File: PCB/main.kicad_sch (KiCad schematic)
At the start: 11 parts, among them Q3 BC337, SW1 config, U1 ESP32-S2-DevKitM

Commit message: First uncompleted release
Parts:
- U1: footprint PCM_Espressif:ESP32-S2-DevKitM -> esp32_dk:ESP32-S2-DevKitM
- renumbered Q3 to Q1, R2 to R1, R7 to R2, R6 to R5
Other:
- added sheet Front outputs (mbes_front_outputs.kicad_sch)
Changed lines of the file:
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@@
 		(on_board yes)
 		(dnp no)
-		(property "Reference" "#PWR01"
+		(property "Reference" "#PWR02"
 			(at 173.99 42.926 0)
 			(effects
@@
 			(project "pcb-a"
 				(path "/709d0967-afe5-49d3-92a5-d2bb94550bdb"
-					(reference "#PWR01")
+					(reference "#PWR02")
 					(unit 1)
 				)
@@
 		(on_board yes)
 		(dnp no)
-		(property "Reference" "R7"
+		(property "Reference" "R2"
 			(at 180.594 50.0888 90)
 			(effects
@@
 			(project "pcb-a"
 				(path "/709d0967-afe5-49d3-92a5-d2bb94550bdb"
-					(reference "R7")
+					(reference "R2")
 					(unit 1)
 				)
@@
 			)
 		)
-		(property "Footprint" "PCM_Espressif:ESP32-S2-DevKitM"
+		(property "Footprint" "esp32_dk:ESP32-S2-DevKitM"
 			(at 135.128 147.32 0)
 			(effects
@@
 		(on_board yes)
 		(dnp no)
-		(property "Reference" "#PWR0104"
+		(property "Reference" "#PWR04"
 			(at 233.172 109.22 0)
 			(effects
@@
 			(project "pcb-a"
 				(path "/709d0967-afe5-49d3-92a5-d2bb94550bdb"
-					(reference "#PWR0104")
+					(reference "#PWR04")
 					(unit 1)
 				)
@@
 		(on_board yes)
 		(dnp no)
-		(property "Reference" "R2"
+		(property "Reference" "R1"
 			(at 117.602 45.1612 90)
 			(effects
@@
 			(project "pcb-a"
 				(path "/709d0967-afe5-49d3-92a5-d2bb94550bdb"
-					(reference "R2")
+					(reference "R1")
 					(unit 1)
 				)
@@
 		(on_board yes)
 		(dnp no)
-		(property "Reference" "R6"
+		(property "Reference" "R5"
 			(at 209.296 27.6352 90)
 			(effects
@@
 			(project "pcb-a"
 				(path "/709d0967-afe5-49d3-92a5-d2bb94550bdb"
-					(reference "R6")
+					(reference "R5")
 					(unit 1)
 				)
@@
 		(on_board yes)
 		(dnp no)
-		(property "Reference" "#PWR02"
+		(property "Reference" "#PWR03"
 			(at 188.976 62.23 0)
 			(effects
@@
 			(project "pcb-a"
 				(path "/709d0967-afe5-49d3-92a5-d2bb94550bdb"
-					(reference "#PWR02")
+					(reference "#PWR03")
 					(unit 1)
 				)
@@
 		(on_board yes)
 		(dnp no)
-		(property "Reference" "Q3"
+		(property "Reference" "Q1"
 			(at 189.2301 30.8864 0)
 			(effects
@@
 			(project "pcb-a"
 				(path "/709d0967-afe5-49d3-92a5-d2bb94550bdb"
-					(reference "Q3")
+					(reference "Q1")
 					(unit 1)
 				)
@@
 		(on_board yes)
 		(dnp no)
-		(property "Reference" "#PWR0103"
+		(property "Reference" "#PWR01"
 			(at 132.588 150.114 0)
 			(effects
@@
 			(project "pcb-a"
 				(path "/709d0967-afe5-49d3-92a5-d2bb94550bdb"
-					(reference "#PWR0103")
+					(reference "#PWR01")
 					(unit 1)
 				)
@@
 	)
 	(sheet
-		(at 22.098 20.066)
-		(size 33.02 9.144)
+		(at 61.468 20.066)
+		(size 29.21 9.144)
 		(exclude_from_sim no)
 		(in_bom yes)
@@
 			(color 0 0 0 0.0000)
 		)
+		(property "Sheetname" "Front outputs"
+			(at 61.468 19.3544 0)
+			(effects
+				(font
+					(size 1.27 1.27)
+				)
+				(justify left bottom)
+			)
+		)
+		(property "Sheetfile" "mbes_front_outputs.kicad_sch"
+			(at 61.468 29.7946 0)
+			(effects
+				(font
+					(size 1.27 1.27)
+				)
+				(justify left top)
+			)
+		)
+		(instances
+			(project "main"
+				(path "/709d0967-afe5-49d3-92a5-d2bb94550bdb"
+					(page "3")
+				)
+			)
+		)
+	)
+	(sheet
+		(at 22.098 20.066)
+		(size 33.02 9.144)
+		(exclude_from_sim no)
+		(in_bom yes)
+		(on_board yes)
+		(dnp no)
+		(fields_autoplaced yes)
+		(stroke
+			(width 0.1524)
+			(type solid)
+		)
+		(fill
+			(color 0 0 0 0.0000)
+		)
 		(property "Sheetname" "mbes_pcbA_connectors"
 			(at 22.098 19.3544 0)
@@
 		)
 		(instances
-			(project "pcb-a"
+			(project "main"
 				(path "/709d0967-afe5-49d3-92a5-d2bb94550bdb"
 					(page "3")

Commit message: Enhancement: the last BC337 has been replaced by a BC817
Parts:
- removed Q1: BC337, Package_TO_SOT_THT:TO-92_Inline_Wide, symbol Transistor_BJT:BC337
- added Q19: BC817, Package_TO_SOT_SMD:SOT-23, symbol Transistor_BJT:BC817
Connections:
- net GND: now also Q19.2 (E)
- net c_startEngine: now also Q19.3 (C)
- net at R2.1: now also Q19.1 (B)
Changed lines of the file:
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@@
-	)
-	(symbol
-		(lib_id "Transistor_BJT:BC337")
-		(at 187.96 35.814 270)
-		(mirror x)
-		(unit 1)
-		(exclude_from_sim no)
-		(in_bom yes)
-		(on_board yes)
-		(dnp no)
-		(property "Reference" "Q1"
-			(at 189.2301 30.8864 0)
-			(effects
-				(font
-					(size 1.27 1.27)
-				)
-				(justify left)
-				(hide yes)
-			)
-		)
-		(property "Value" "BC337"
-			(at 184.658 30.5308 90)
-			(effects
-				(font
-					(size 1.27 1.27)
-				)
-				(justify left)
-			)
-		)
-		(property "Footprint" "Package_TO_SOT_THT:TO-92_Inline_Wide"
-			(at 186.055 30.734 0)
-			(effects
-				(font
-					(size 1.27 1.27)
-					(italic yes)
-				)
-				(justify left)
-				(hide yes)
-			)
-		)
-		(property "Datasheet" "https://diotec.com/tl_files/diotec/files/pdf/datasheets/bc337.pdf"
-			(at 187.96 35.814 0)
-			(effects
-				(font
-					(size 1.27 1.27)
-				)
-				(justify left)
-				(hide yes)
-			)
-		)
-		(property "Description" ""
-			(at 187.96 35.814 0)
-			(effects
-				(font
-					(size 1.27 1.27)
-				)
-				(hide yes)
-			)
-		)
-		(pin "1"
-		)
-		(pin "2"
-		)
-		(pin "3"
-		)
-		(instances
-			(project "pcb-a"
-				(path "/709d0967-afe5-49d3-92a5-d2bb94550bdb"
-					(reference "Q1")
-					(unit 1)
-				)
-			)
-		)
 	)
 	(symbol
@@
 					(unit 1)
 				)
+			)
+		)
+	)
+	(symbol
+		(lib_id "Transistor_BJT:BC817")
+		(at 187.96 35.814 270)
+		(mirror x)
+		(unit 1)
+		(exclude_from_sim no)
+		(in_bom yes)
+		(on_board yes)
+		(dnp no)
+		(fields_autoplaced yes)
+		(property "Reference" "Q19"
+			(at 187.96 26.416 90)
+			(effects
+				(font
+					(size 1.27 1.27)
+				)
+				(hide yes)
+			)
+		)
+		(property "Value" "BC817"
+			(at 187.96 28.956 90)
+			(effects
+				(font
+					(size 1.27 1.27)
+				)
+			)
+		)
+		(property "Footprint" "Package_TO_SOT_SMD:SOT-23"
+			(at 186.055 30.734 0)
+			(effects
+				(font
+					(size 1.27 1.27)
+					(italic yes)
+				)
+				(justify left)
+				(hide yes)
+			)
+		)
+		(property "Datasheet" "https://www.onsemi.com/pub/Collateral/BC818-D.pdf"
+			(at 187.96 35.814 0)
+			(effects
+				(font
+					(size 1.27 1.27)
+				)
+				(justify left)
+				(hide yes)
+			)
+		)
+		(property "Description" "0.8A Ic, 45V Vce, NPN Transistor, SOT-23"
+			(at 187.96 35.814 0)
+			(effects
+				(font
+					(size 1.27 1.27)
+				)
+				(hide yes)
+			)
+		)
+		(pin "2"
+		)
+		(pin "1"
+		)
+		(pin "3"
+		)
+		(instances
+			(project ""
+				(path "/709d0967-afe5-49d3-92a5-d2bb94550bdb"
+					(reference "Q19")
+					(unit 1)
+				)

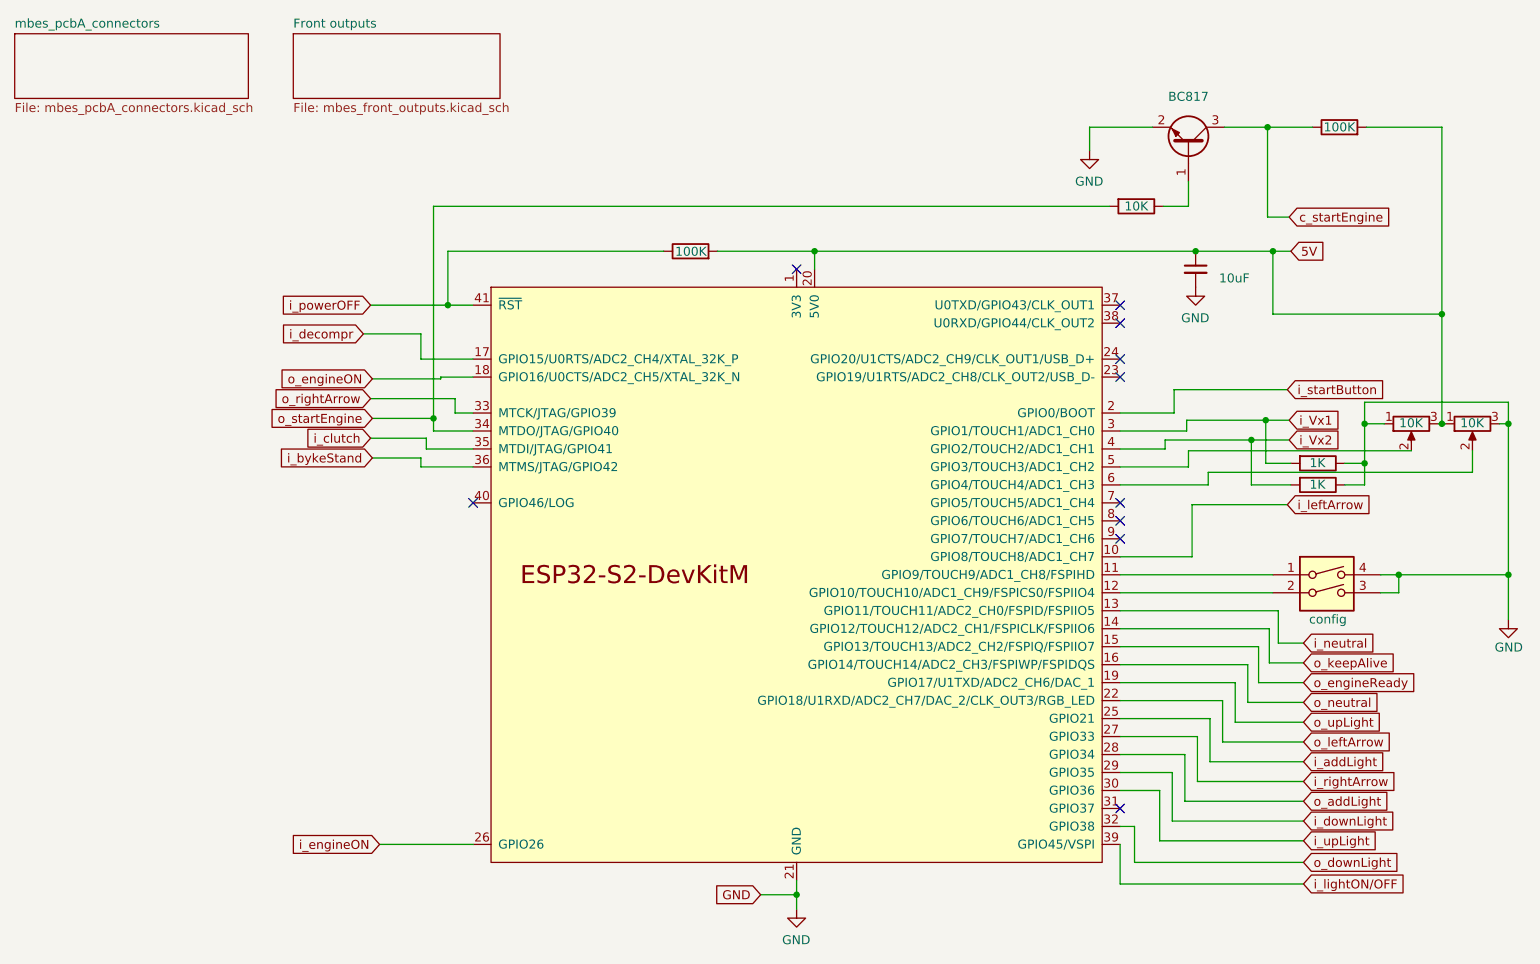
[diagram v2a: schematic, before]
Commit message: Many fixes and changes
- Electric schema and PCB changes:
	- To avoid unwanted service starting (lights, electric start engine....), the signals from the motorbike's front side to
	  the rear one, are no more connedted to the FET's gate directly. There is a second stage realized with PNPs transistors,
	  now. It is a more stable and safe solution.

- In the shcema:
	- All the c_<signal> symbols have been splitted in ci_<signal> and co_<signal>, and the symbols direction (input/output)
	  have been fixed
	- To get a more readable schema, the c*_<signal> symbols have a different color
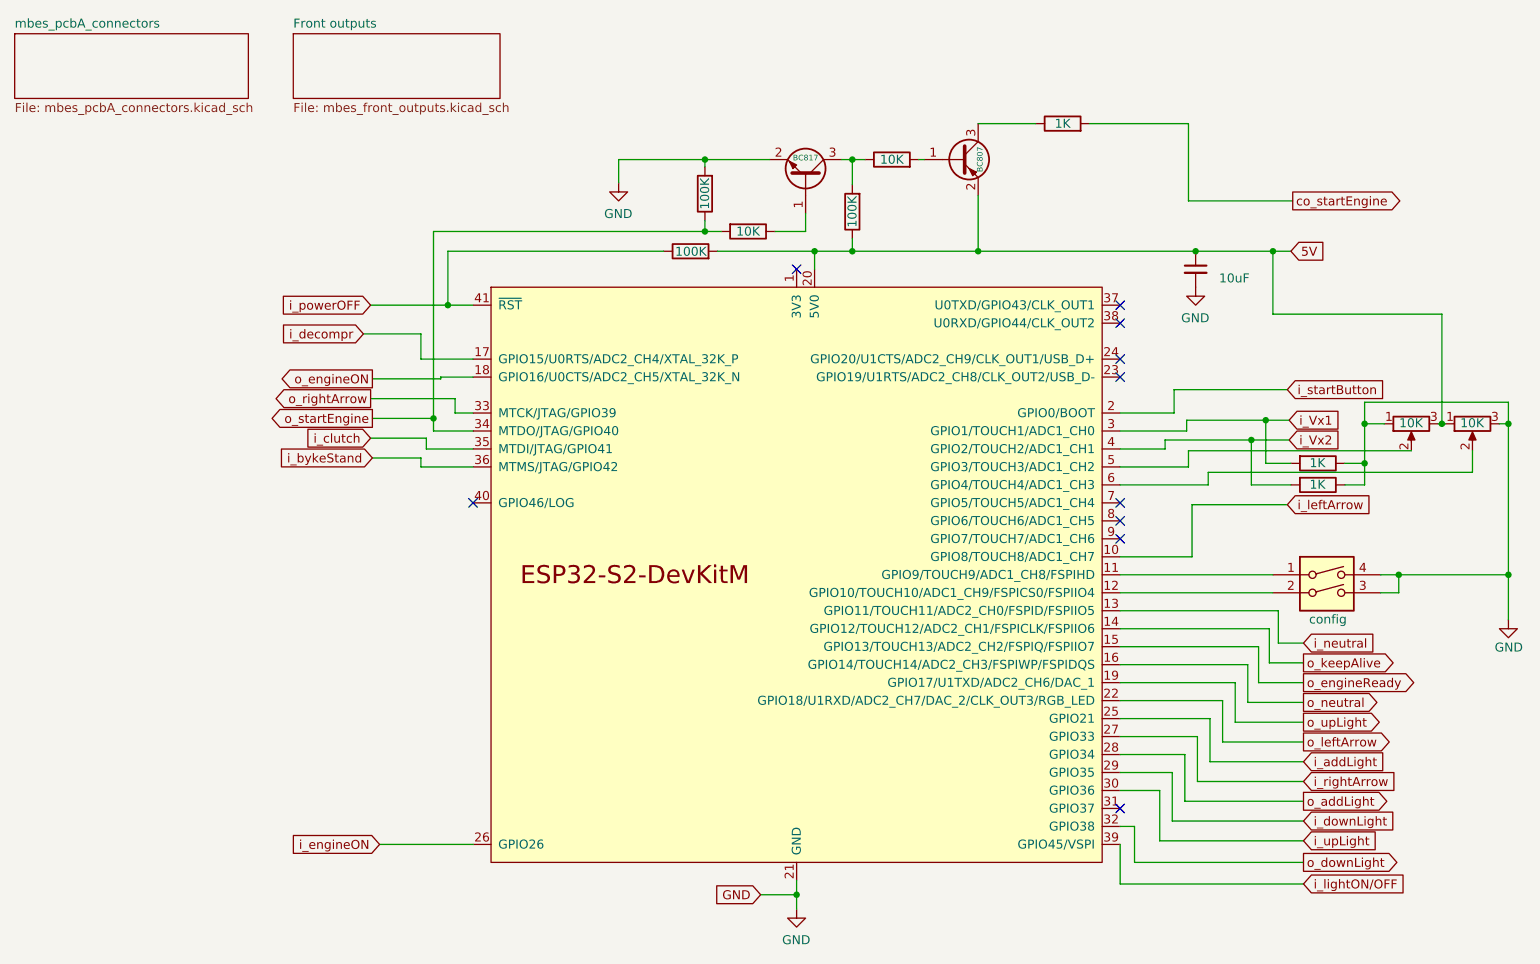
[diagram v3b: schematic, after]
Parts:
- added Q23: BC807, Package_TO_SOT_SMD:SOT-23, symbol Transistor_BJT:BC807
- added R14: 100K, Resistor_SMD:R_1206_3216Metric, symbol Device:R
- added RA49: 10K, Resistor_SMD:R_1206_3216Metric, symbol Device:R
- added RA51: 1K, Resistor_SMD:R_1206_3216Metric, symbol Device:R
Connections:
- net 5V: now also R5.1, Q23.2 (E); no longer R5.2
- net GND: now also R14.2
- net o_startEngine: now also R14.1
- net c_startEngine: no longer names the net of Q19.3 (C)
- net c_startEngine: now also R5.2, RA49.1; no longer R5.1
- new net: Q23.1 (B), RA49.2
- new net: Q23.3 (C), RA51.1
- new net co_startEngine: RA51.2

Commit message: Merge from ESP32__dualPCB branch
- DownLight: external fuse replaced by internal automatic one, wire connector replaced by 2.54 pin-header
- The resistor between FET's gate and NPN's collector has been removed
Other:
- company: Panicosoft -> https://github.com/catinella/mbElectricalSystem
- title: Motorbike lights and services controller -> (front side) Motorbike Electrical System
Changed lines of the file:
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@@
 	(paper "A4")
 	(title_block
-		(title "Motorbike lights and services controller")
-		(date "2022-08-24")
-		(rev "4.0")
-		(company "Panicosoft")
-		(comment 1 "Logic controller unit")
-		(comment 2 "MCU connections")
+		(title "(front side) Motorbike Electrical System")
+		(company "https://github.com/catinella/mbElectricalSystem")
 	)
 	(bus_alias "port-b"
